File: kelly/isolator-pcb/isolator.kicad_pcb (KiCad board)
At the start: 2 copper layers, 50 x 32 mm, 19 parts

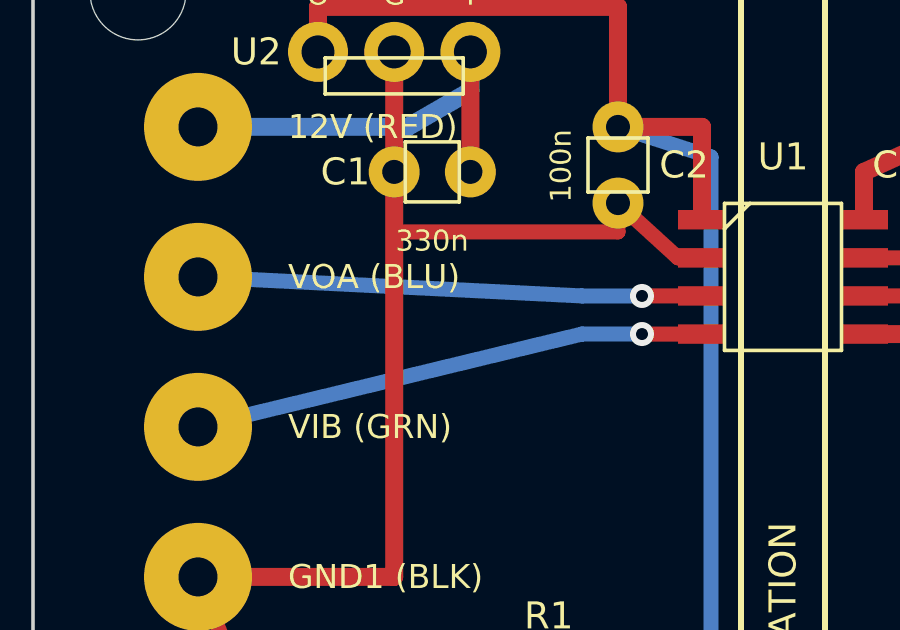
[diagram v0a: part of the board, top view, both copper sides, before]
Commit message: Fix ADuM1201 side-1 pinout on the isolator PCB (rev B)
The U1 pin table assumed side 1 mirrored side 2 (VDD1, GND1, sig, sig), but
the ADuM1201 puts GND1 on pin 4: side 1 is VDD1, VOA, VIB, GND1 top to
bottom (datasheet Rev. L Fig. 5). Rev A therefore routed GND1 onto pin 2 and
shifted VOA/VIB down one, shorting VOA (an output) to GND1 on power-up. Side
2 was already correct. No chip orientation recovers rev A.

Reroute side 1 to suit: signal vias move to the pin 2/3 rows at x=20.6, and
GND1 tees off the C2 spur at (19.5, 11.5) and comes into pin 4 from below,
west of the via column so nothing crosses. DRC: 0 violations, 0 unconnected.

DRC passed rev A because one wrong table generated both the pads and the
netlist, leaving nothing to compare against. Add ADUM1201, a literal
transcription of the datasheet pinout, and assert every pad's net against it
at generate time -- it reproduces the rev A failure when reverted.

Regenerate the board, gerbers, drill map, fab zip, and both renders. README
gets a rev A erratum with the 3-cut/3-jumper rework for the fabbed boards,
and the render + zip commands that were missing from the regenerate block.

Co-Authored-By: Claude Opus 5 <noreply@anthropic.com>
Claude-Session: https://claude.ai/code/session_01UdkbaD5XWcGgk61KsSv1pw
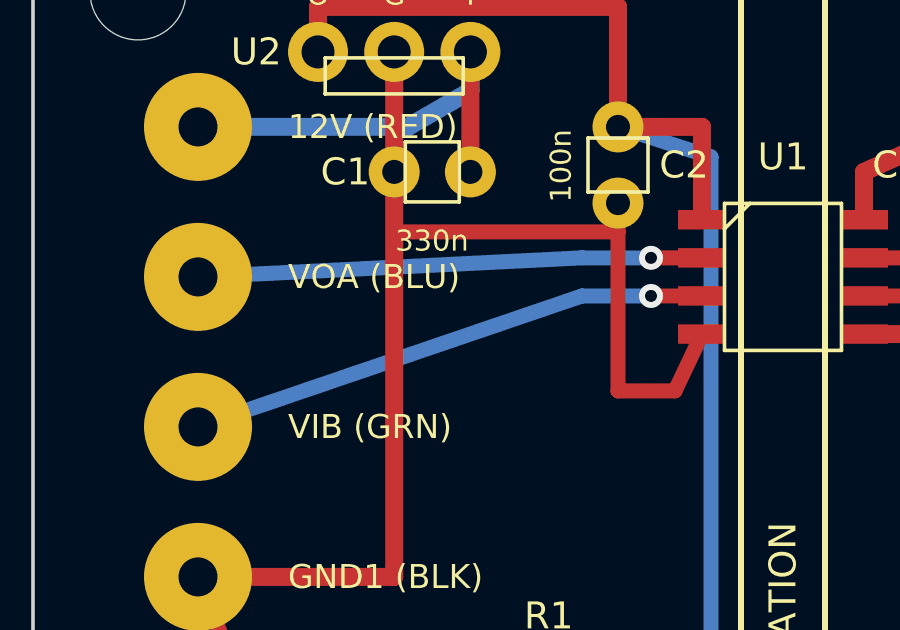
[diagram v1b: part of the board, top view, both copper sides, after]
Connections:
- U1 pad 2: GND1 -> VOA
- U1 pad 3: VOA -> VIB
- U1 pad 4: VIB -> GND1
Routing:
- net GND1: track 41.3 -> 47.1 mm
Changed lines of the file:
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@@
   (fp_text value "" (at 0 0) (layer "F.Fab") hide (effects (font (size 0.9 0.9) (thickness 0.15))))
   (pad "1" smd rect (at -2.700 -1.905) (size 1.6 0.65) (layers "F.Cu" "F.Paste" "F.Mask") (net 3 "+5V_K"))
-  (pad "2" smd rect (at -2.700 -0.635) (size 1.6 0.65) (layers "F.Cu" "F.Paste" "F.Mask") (net 2 "GND1"))
-  (pad "3" smd rect (at -2.700 0.635) (size 1.6 0.65) (layers "F.Cu" "F.Paste" "F.Mask") (net 5 "VOA"))
-  (pad "4" smd rect (at -2.700 1.905) (size 1.6 0.65) (layers "F.Cu" "F.Paste" "F.Mask") (net 4 "VIB"))
+  (pad "2" smd rect (at -2.700 -0.635) (size 1.6 0.65) (layers "F.Cu" "F.Paste" "F.Mask") (net 5 "VOA"))
+  (pad "3" smd rect (at -2.700 0.635) (size 1.6 0.65) (layers "F.Cu" "F.Paste" "F.Mask") (net 4 "VIB"))
+  (pad "4" smd rect (at -2.700 1.905) (size 1.6 0.65) (layers "F.Cu" "F.Paste" "F.Mask") (net 2 "GND1"))
   (pad "5" smd rect (at 2.700 1.905) (size 1.6 0.65) (layers "F.Cu" "F.Paste" "F.Mask") (net 7 "GND2"))
   (pad "6" smd rect (at 2.700 0.635) (size 1.6 0.65) (layers "F.Cu" "F.Paste" "F.Mask") (net 8 "VOB"))
@@
 (segment (start 112.040 61.500) (end 119.500 61.500) (width 0.5) (layer "F.Cu") (net 2))
 (segment (start 119.500 61.500) (end 119.500 60.540) (width 0.5) (layer "F.Cu") (net 2))
-(segment (start 119.500 60.540) (end 121.500 62.365) (width 0.5) (layer "F.Cu") (net 2))
-(segment (start 121.500 62.365) (end 122.300 62.365) (width 0.5) (layer "F.Cu") (net 2))
+(segment (start 119.500 61.500) (end 119.500 66.800) (width 0.5) (layer "F.Cu") (net 2))
+(segment (start 119.500 66.800) (end 121.400 66.800) (width 0.5) (layer "F.Cu") (net 2))
+(segment (start 121.400 66.800) (end 122.300 64.905) (width 0.5) (layer "F.Cu") (net 2))
 (segment (start 114.580 59.500) (end 114.580 55.500) (width 0.6) (layer "F.Cu") (net 1))
-(segment (start 105.500 63.000) (end 118.300 63.635) (width 0.5) (layer "B.Cu") (net 5))
-(segment (start 118.300 63.635) (end 120.300 63.635) (width 0.5) (layer "B.Cu") (net 5))
-(via (at 120.300 63.635) (size 0.8) (drill 0.4) (layers "F.Cu" "B.Cu") (net 5))
-(segment (start 120.300 63.635) (end 122.300 63.635) (width 0.5) (layer "F.Cu") (net 5))
-(segment (start 105.500 68.000) (end 118.300 64.905) (width 0.5) (layer "B.Cu") (net 4))
-(segment (start 118.300 64.905) (end 120.300 64.905) (width 0.5) (layer "B.Cu") (net 4))
-(via (at 120.300 64.905) (size 0.8) (drill 0.4) (layers "F.Cu" "B.Cu") (net 4))
-(segment (start 120.300 64.905) (end 122.300 64.905) (width 0.5) (layer "F.Cu") (net 4))
+(segment (start 105.500 63.000) (end 118.300 62.365) (width 0.5) (layer "B.Cu") (net 5))
+(segment (start 118.300 62.365) (end 120.600 62.365) (width 0.5) (layer "B.Cu") (net 5))
+(via (at 120.600 62.365) (size 0.8) (drill 0.4) (layers "F.Cu" "B.Cu") (net 5))
+(segment (start 120.600 62.365) (end 122.300 62.365) (width 0.5) (layer "F.Cu") (net 5))
+(segment (start 105.500 68.000) (end 118.300 63.635) (width 0.5) (layer "B.Cu") (net 4))
+(segment (start 118.300 63.635) (end 120.600 63.635) (width 0.5) (layer "B.Cu") (net 4))
+(via (at 120.600 63.635) (size 0.8) (drill 0.4) (layers "F.Cu" "B.Cu") (net 4))
+(segment (start 120.600 63.635) (end 122.300 63.635) (width 0.5) (layer "F.Cu") (net 4))
 (segment (start 144.500 58.000) (end 131.000 58.000) (width 0.6) (layer "F.Cu") (net 6))
 (segment (start 131.000 58.000) (end 127.700 59.500) (width 0.6) (layer "F.Cu") (net 6))
